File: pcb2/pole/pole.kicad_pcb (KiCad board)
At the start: 2 copper layers, 17 x 49 mm, 21 parts, among them IC1 LMx93, IC2 STM32F0xxKxTx, P1 POWER_IN, P2 BUS_IN, P3 BUS_OUT, P4 SWD_TC, P5 LEDs, Q1 MTM232270LBF, Q2 MTM232270LBF, Q3 MTM232270LBF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

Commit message: Use STM32F051, changed FPs to agg-kicad
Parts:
- IC2: value STM32F0xxKxTx -> STM32F0xxKxUx; footprint agg:LQFP-32 -> agg:QFN-32-EP-ST
- Q1, Q2, Q3, Q4: footprint thegrid:SOT-323 -> agg:SOT-323
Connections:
- IC1 pad 7: Net-(IC1-Pad7) -> (no net)
- IC2 pad 10: Net-(IC2-Pad10) -> /PIEZO
- IC2 pad 11: Net-(IC2-Pad11) -> (no net)
- IC2 pad 12: Net-(IC2-Pad12) -> (no net)
- IC2 pad 13: Net-(IC2-Pad13) -> (no net)
- IC2 pad 14: Net-(IC2-Pad14) -> (no net)
- IC2 pad 15: Net-(IC2-Pad15) -> (no net)
- IC2 pad 16: GND -> (no net)
- IC2 pad 17: +3V3 -> (no net)
- IC2 pad 18: Net-(IC2-Pad18) -> (no net)
- IC2 pad 19: Net-(IC2-Pad19) -> (no net)
- IC2 pad 2: Net-(IC2-Pad2) -> (no net)
- IC2 pad 20: Net-(IC2-Pad20) -> (no net)
- IC2 pad 21: Net-(IC2-Pad21) -> (no net)
- IC2 pad 22: Net-(IC2-Pad22) -> (no net)
- IC2 pad 25: Net-(IC2-Pad25) -> (no net)
- IC2 pad 26: Net-(IC2-Pad26) -> (no net)
- IC2 pad 27: Net-(IC2-Pad27) -> (no net)
- IC2 pad 28: Net-(IC2-Pad28) -> (no net)
- IC2 pad 29: Net-(IC2-Pad29) -> (no net)
- IC2 pad 3: Net-(IC2-Pad3) -> (no net)
- IC2 pad 30: Net-(IC2-Pad30) -> (no net)
- IC2 pad 32: GND -> (no net)
- IC2 pad 5: +3V3 -> (no net)
- IC2 pad 6: Net-(IC2-Pad6) -> (no net)
- IC2 pad 7: Net-(IC2-Pad7) -> (no net)
- IC2 pad 8: Net-(IC2-Pad8) -> (no net)
- IC2 pad 9: Net-(IC2-Pad9) -> (no net)
- P4 pad 6: Net-(P4-Pad6) -> (no net)
- Q1 pad 1: /LED_R -> (no net)
- Q2 pad 1: /LED_G -> (no net)
- Q3 pad 1: /LED_B -> (no net)

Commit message: Finished pin assignments, first layout
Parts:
- added C8: 1u, agg:0603, F.Cu at (117.0, 81.2)
- C2: value C_Small -> 4u7
- C3, C5: value C_Small -> 100n
- C4: value C_Small -> 10n
- moved C2 36.2 mm to (117.0, 76.8), turned to 90 degrees
- moved C3 27.8 mm to (118.5, 76.8), turned to 90 degrees
- moved C4 27.3 mm to (118.5, 81.2), turned to 270 degrees
- moved C5 23.4 mm to (126.0, 80.5), turned to 90 degrees
- moved Q4 6.73 mm to (122.8, 84.0), turned to 0 degrees
- moved C7 2.80 mm to (120.8, 91.5), turned to 0 degrees
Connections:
- C2 pad 1: GND -> Net-(C2-Pad1)
- C2 pad 2: +3V3 -> GND
- C3 pad 1: GND -> Net-(C2-Pad1)
- C3 pad 2: +3V3 -> GND
- C4 pad 1: GND -> Net-(C4-Pad1)
- C4 pad 2: +3V3 -> GND
- C5 pad 1: GND -> Net-(C5-Pad1)
- C5 pad 2: /NRST -> GND
- IC2 pad 1: (no net) -> Net-(C2-Pad1)
- IC2 pad 17: (no net) -> Net-(C5-Pad1)
- IC2 pad 18: (no net) -> /LED_R
- IC2 pad 19: (no net) -> /LED_G
- IC2 pad 20: (no net) -> /LED_B
- IC2 pad 5: (no net) -> Net-(C4-Pad1)
- IC2 pad 9: (no net) -> /BUS
- Q1 pad 1: (no net) -> /LED_R
- Q2 pad 1: (no net) -> /LED_G
- Q3 pad 1: (no net) -> /LED_B

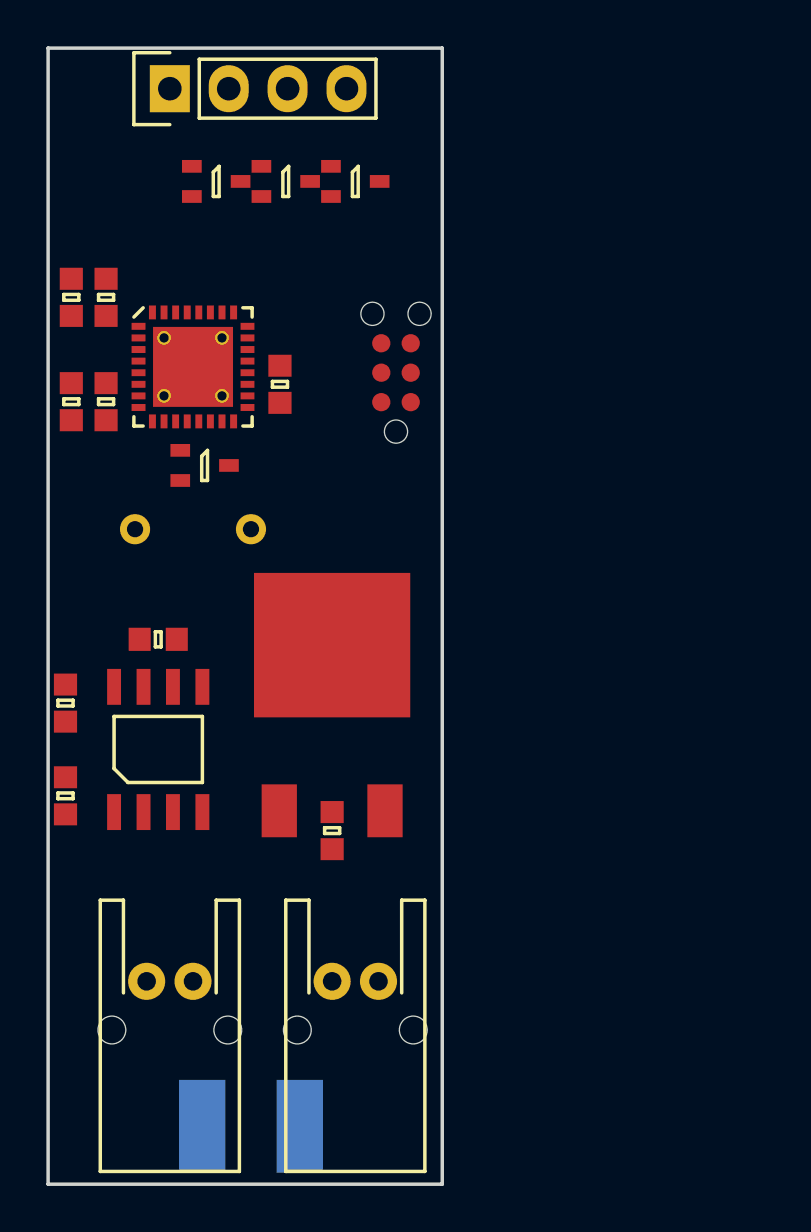
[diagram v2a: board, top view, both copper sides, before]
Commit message: First proof of concept route, with gerbers
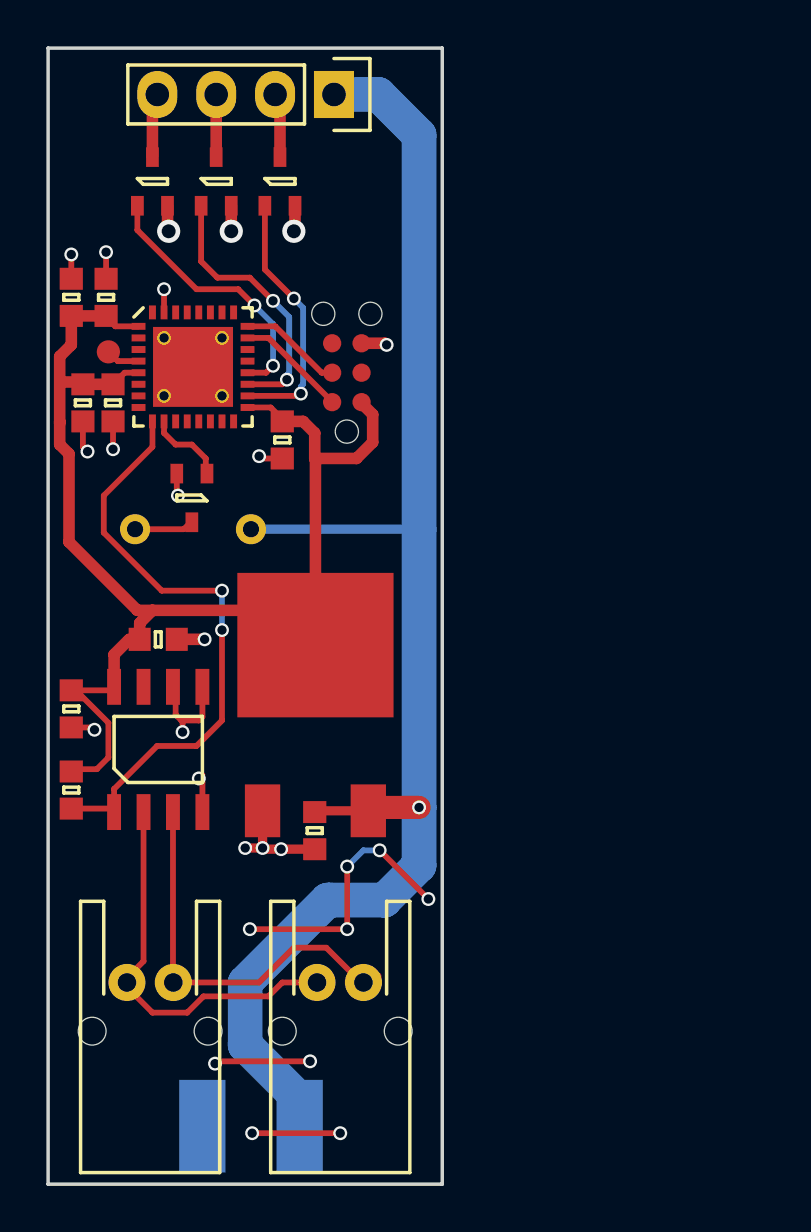
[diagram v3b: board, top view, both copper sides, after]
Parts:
- added TP1: RST, agg:TESTPAD, F.Cu at (118.6, 79.1)
- moved Q3 8.75 mm to (120.5, 71.8), turned to 90 degrees
- moved P5 7.08 mm to (128.3, 68.0), turned to 270 degrees
- moved Q2 3.00 mm to (123.2, 71.8), turned to 90 degrees
- moved Q1 2.75 mm to (126.0, 71.8), turned to 90 degrees
- moved C5 2.40 mm to (126.1, 82.9), turned to 270 degrees
- moved P4 2.12 mm to (128.9, 80.0)
- moved Q4 1.50 mm to (122.2, 85.4), turned to 270 degrees
- moved P2 0.85 mm to (120.4, 106.3)
- moved C6 0.75 mm to (127.5, 99.8)
- moved U1 0.72 mm to (127.5, 91.8)
- moved P3 0.65 mm to (128.6, 106.3)
- moved C8 0.50 mm to (117.5, 81.3)
- moved C1 0.35 mm to (117.0, 94.5)
- moved R1 0.35 mm to (117.0, 98.0)
- moved C4 0.30 mm to (118.8, 81.3)
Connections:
- C2 pad 1: Net-(C2-Pad1) -> +3V3
- C3 pad 1: Net-(C2-Pad1) -> +3V3
- C4 pad 1: Net-(C4-Pad1) -> +3V3
- C5 pad 1: Net-(C5-Pad1) -> +3V3
- C8 pad 1: Net-(C4-Pad1) -> +3V3
- IC2 pad 1: Net-(C2-Pad1) -> +3V3
- IC2 pad 17: Net-(C5-Pad1) -> +3V3
- IC2 pad 4: /NRST -> Net-(IC2-Pad4)
- IC2 pad 5: Net-(C4-Pad1) -> +3V3
- P4 pad 3: /NRST -> (no net)
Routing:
- net +12V: track 0.00 -> 64.7 mm, vias 0 -> 1
- net +3V3: track 0.00 -> 58.5 mm
- net GND: track 0.00 -> 46.5 mm, vias 0 -> 27
- net /BUS: track 0.00 -> 26.3 mm, vias 0 -> 2
- net /BUS_B: track 0.00 -> 17.5 mm
- net /BUS_A: track 0.00 -> 17.1 mm
- net /LED_G: track 0.00 -> 11.7 mm, vias 0 -> 2
- net /LED_B: track 0.00 -> 11.6 mm, vias 0 -> 2
- net /LED_R: track 0.00 -> 11.2 mm, vias 0 -> 2
- net /SWDIO: track 0.00 -> 4.81 mm
- net /SWDCLK: track 0.00 -> 4.48 mm
- net /PIEZO: track 0.00 -> 3.41 mm
- net /DRIVE_R: track 0.00 -> 2.79 mm
- net /DRIVE_B: track 0.00 -> 2.79 mm
- net /DRIVE_G: track 0.00 -> 2.70 mm
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- added copper zone on B.Cu, net GND
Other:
- net class Default: clearance 0.2 -> 0.15
- rule pad_to_mask_clearance: 0.2 -> 0
- rule trace_clearance: 0.2 -> 0.15
- rule trace_min: 0.2 -> 0.25
- rule via_min_drill: 0.3 -> 0.4
- rule via_min_size: 0.4 -> 0.6

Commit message: Added board-outline
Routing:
- net (no net): track 0.00 -> 19.5 mm, vias 0 -> 9
- net GND: track 46.5 -> 27.0 mm, vias 27 -> 18
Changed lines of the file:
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@@
     (visible_elements FFFFFF7F)
     (pcbplotparams
-      (layerselection 0x000f8_80000001)
+      (layerselection 0x010f8_80000001)
       (usegerberextensions true)
       (excludeedgelayer true)
@@
   (gr_line (start 133 115) (end 133 66) (angle 90) (layer Edge.Cuts) (width 0.15))
   (gr_line (start 116 66) (end 116 115) (angle 90) (layer Edge.Cuts) (width 0.15))
-  (via (at 124.8 112.8) (size 0.6) (drill 0.4) (layers F.Cu B.Cu) (net 1))
-  (via (at 128.6 112.8) (size 0.6) (drill 0.4) (layers F.Cu B.Cu) (net 1))
-  (segment (start 124.8 112.8) (end 128.6 112.8) (width 0.25) (layer F.Cu) (net 1))
-  (via (at 123.2 109.8) (size 0.6) (drill 0.4) (layers F.Cu B.Cu) (net 1))
-  (via (at 127.3 109.7) (size 0.6) (drill 0.4) (layers F.Cu B.Cu) (net 1))
-  (segment (start 127.3 109.7) (end 123.3 109.7) (width 0.25) (layer F.Cu) (net 1))
-  (segment (start 123.3 109.7) (end 123.2 109.8) (width 0.25) (layer F.Cu) (net 1))
-  (segment (start 124.7 104) (end 128.9 104) (width 0.25) (layer F.Cu) (net 1))
-  (segment (start 129.6 100.6) (end 128.9 101.3) (width 0.25) (layer B.Cu) (net 1))
-  (via (at 128.9 101.3) (size 0.6) (drill 0.4) (layers F.Cu B.Cu) (net 1))
-  (segment (start 128.9 101.3) (end 128.9 104) (width 0.25) (layer F.Cu) (net 1))
-  (via (at 128.9 104) (size 0.6) (drill 0.4) (layers F.Cu B.Cu) (net 1))
-  (via (at 130.3 100.6) (size 0.6) (drill 0.4) (layers F.Cu B.Cu) (net 1))
-  (via (at 132.4 102.7) (size 0.6) (drill 0.4) (layers F.Cu B.Cu) (net 1))
-  (segment (start 130.3 100.6) (end 132.4 102.7) (width 0.25) (layer F.Cu) (net 1))
-  (segment (start 130.3 100.6) (end 129.6 100.6) (width 0.25) (layer B.Cu) (net 1))
-  (via (at 124.7 104) (size 0.6) (drill 0.4) (layers F.Cu B.Cu) (net 1))
+  (via (at 124.8 112.8) (size 0.6) (drill 0.4) (layers F.Cu B.Cu) (net 0))
+  (via (at 128.6 112.8) (size 0.6) (drill 0.4) (layers F.Cu B.Cu) (net 0))
+  (segment (start 124.8 112.8) (end 128.6 112.8) (width 0.25) (layer F.Cu) (net 0))
+  (via (at 123.2 109.8) (size 0.6) (drill 0.4) (layers F.Cu B.Cu) (net 0))
+  (via (at 127.3 109.7) (size 0.6) (drill 0.4) (layers F.Cu B.Cu) (net 0))
+  (segment (start 127.3 109.7) (end 123.3 109.7) (width 0.25) (layer F.Cu) (net 0))
+  (segment (start 123.3 109.7) (end 123.2 109.8) (width 0.25) (layer F.Cu) (net 0))
+  (segment (start 124.7 104) (end 128.9 104) (width 0.25) (layer F.Cu) (net 0))
+  (segment (start 129.6 100.6) (end 128.9 101.3) (width 0.25) (layer B.Cu) (net 0))
+  (via (at 128.9 101.3) (size 0.6) (drill 0.4) (layers F.Cu B.Cu) (net 0))
+  (segment (start 128.9 101.3) (end 128.9 104) (width 0.25) (layer F.Cu) (net 0))
+  (via (at 128.9 104) (size 0.6) (drill 0.4) (layers F.Cu B.Cu) (net 0))
+  (via (at 130.3 100.6) (size 0.6) (drill 0.4) (layers F.Cu B.Cu) (net 0))
+  (via (at 132.4 102.7) (size 0.6) (drill 0.4) (layers F.Cu B.Cu) (net 0))
+  (segment (start 130.3 100.6) (end 132.4 102.7) (width 0.25) (layer F.Cu) (net 0))
+  (segment (start 130.3 100.6) (end 129.6 100.6) (width 0.25) (layer B.Cu) (net 0))
+  (via (at 124.7 104) (size 0.6) (drill 0.4) (layers F.Cu B.Cu) (net 0))
   (segment (start 117 95.3) (end 117.9 95.3) (width 0.25) (layer F.Cu) (net 1))
   (via (at 118 95.4) (size 0.6) (drill 0.4) (layers F.Cu B.Cu) (net 1))
@@
   (segment (start 118.695 98.8) (end 118.845 98.95) (width 0.25) (layer F.Cu) (net 4))
   (segment (start 116.85 98.95) (end 116.75 99.05) (width 0.25) (layer F.Cu) (net 4))
-  (segment (start 127.6 106.3) (end 126.1 106.3) (width 0.25) (layer F.Cu) (net 5) (status 400000))
-  (segment (start 120.5 107.6) (end 119.4 106.5) (width 0.25) (layer F.Cu) (net 5) (status 800000))
+  (segment (start 127.6 106.3) (end 126.1 106.3) (width 0.25) (layer F.Cu) (net 5))
+  (segment (start 120.5 107.6) (end 119.4 106.5) (width 0.25) (layer F.Cu) (net 5))
   (segment (start 122 107.6) (end 120.5 107.6) (width 0.25) (layer F.Cu) (net 5))
   (segment (start 122.7 106.9) (end 122 107.6) (width 0.25) (layer F.Cu) (net 5))
   (segment (start 125.5 106.9) (end 122.7 106.9) (width 0.25) (layer F.Cu) (net 5))
   (segment (start 126.1 106.3) (end 125.5 106.9) (width 0.25) (layer F.Cu) (net 5))
-  (segment (start 119.4 106.5) (end 119.4 106.3) (width 0.25) (layer F.Cu) (net 5) (status C00000))
+  (segment (start 119.4 106.5) (end 119.4 106.3) (width 0.25) (layer F.Cu) (net 5))
   (segment (start 127.7 106.3) (end 127.6 106.3) (width 0.25) (layer F.Cu) (net 5))
   (segment (start 120.115 98.95) (end 120.115 105.385) (width 0.25) (layer F.Cu) (net 5))
